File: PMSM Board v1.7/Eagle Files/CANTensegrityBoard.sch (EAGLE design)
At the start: 92 parts, among them IC1 DRV8303, U1 TPS73733-Q1_DRB_8, U10 H1206T500R-10, U2 SN65HVD232_D_8, U3 SN65LVDT348_PW_1, U4 TPS54240_DRC_10, U5 LP38692_NGG_6, U6 DSPIC33EP256MU80, U9 H1206T500R-10

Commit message: Finished v1.7
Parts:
- removed SJ1, SJ4, SJ5, SJ6, SJ7: (no value), jumper:SJ
- added JP1: (no value), ASL:M06DUAL_ROW
- added LED5, LED6: (no value), ASL:LED0805
- added R12, R13: 10k, ASL:RESISTOR0805-RES
- added R14, R15: (no value), ASL:RESISTOR0805-RES
- R1: value (none) -> 1 Ohm
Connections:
- removed net EN_A: U3.ROUT1
- removed net EN_A+: U3.RIN1+
- removed net EN_A-: U3.RIN1
- removed net EN_B: U3.ROUT2
- removed net EN_B+: U3.RIN2+
- removed net EN_B-: U3.RIN2
- removed net EN_C: U3.ROUT3
- removed net EN_C+: U3.RIN3+
- removed net EN_C-: U3.RIN3
- removed net N$27: SJ4.2
- removed net N$29: SJ6.2
- removed net N$30: SJ7.2
- removed net N$33: RN1.1
- removed net N$41: RN1.2
- removed net N$42: RN1.3
- removed net N$43: RN1.4
- new net CH_A+: U$15.6, U3.RIN3+
- new net CH_A-: U$15.5, U3.RIN3
- new net CH_B+: U$15.4, U3.RIN2+
- new net CH_B-: U$15.3, U3.RIN2
- new net CH_I+: U$15.2, U3.RIN1+
- new net CH_I-: U$15.1, U3.RIN1
- new net EXT1: JP1.1, U6.PMWR/RP68/RD4
- new net EXT2: JP1.2, U6.PMBE/RP67/RD3
- new net EXT3: JP1.3, U6.DPH/RP66/RD2
- new net HALL1: U$20.3, U6.PGEC2/SOSCO/C3IN1-/T1CK/RPI62/RC14
- new net HALL2: U$20.4, U6.PGED2/SOSCI/C3IN3-/RPI61/RC13
- new net HALL3: U$20.5, U6.INT0/DMH/RP64/RD0
- new net LED1: RN1.4, U6.AN8/PMA6/RPI40/RB8
- new net LED2: RN1.3, U6.AN9/PMA7//RPI41/RB9
- new net LED3: RN1.2, U6.TMS/AN10/CVREF/PMA13/RPI42/RB10
- new net LED4: RN1.1, U6.TDO/AN11/PMA12/RPI43/RB11
- new net N$11: LED5.C, R15.2
- new net N$17: LED6.C, R14.2
- new net N$23: R12.2, U$19.3
- new net QEI_A: U3.ROUT1, U6.C3IN1+/VCMPST3/RP71/RD7
- new net QEI_B: U3.ROUT2, U6.C3IN2-/RP70/RD6
- new net QEI_I: U3.ROUT3, U6.PMRD/RP69/RD5
- net *SCS: now also U6.C2IN1-/PMA2/RPI121/RG9
- net CANRX: now also U6.SDA2/PMA9/RP100/RF4
- net CANTX: now also U6.SCL2/PMA8/RP101/RF5
- net CAN_H: now also U$14.1, U$19.1
- net CAN_L: now also U$14.2, U$19.2
- net CRNT1: now also U6.TCK/AN12/PMA11/RPI44/RB12
- net CRNT2: now also U6.TDI/AN13/PMA10/RPI45/RB13
- net DC_CAL: now also U6.C2IN3-/SDO2/PMA3/RP120/RG8
- net EN_GATE: now also U6.C1IN1-/SDI2/PMA4/RPI119/RG7
- net GND: now also JP1.4, U$15.7, U$20.2, U6.AVSS, U6.VSS, U6.VSS_2, U6.VSS_3
- net MCLR: now also U6.*MCLR
- net MISO: now also U6.AN31/PWM4H/PMD7/RP87/RE7
- net MOSI: now also U6.C1IN3-/SCK2/PMA5/RP118/RG6
- net N$12: now also R14.1
- net N$24: now also R15.1
- net N$25: now also U6.PGEC3/AN1/VREF-/RPI33/RB1
- net N$28: now also R13.2, U$14.3; no longer SJ5.2
- net N$31: now also U6.VCAP
- net N$5: now also U6.VDD_4; no longer SJ1.2
- net PGC: now also U6.PGED1/AN7/RCV/RPI39/RB7
- net PGD: now also U6.PGEC1/AN6/RPI38/RB6
- net PGND: now also U$16.1, U$16.4, U$18.2
- net PVDD: now also U$16.2, U$16.3
- net PWM1H: now also U6.AN29/PWM3H/PMD5/RP85/RE5
- net PWM1L: now also U6.AN28/PWM3L/PMD4/RP84/RE4
- net PWM2H: now also U6.AN27/PWM2H/PMD3/RPI83/RE3
- net PWM2L: now also U6.AN26/PWM2L/PMD2/RP82/RE2
- net PWM3H: now also U6.AN25/PWM1H/PMD1/RPI81/RE1
- net PWM3L: now also U6.AN24/PWM1L/PMD0/RP80/RE0
- net SCLK: now also U6.AN30/PWM4L/PMD6/RPI86/RE6
- net SH_A: now also U$17.5, U$17.6
- net SH_B: now also U$17.3, U$17.4
- net SH_C: now also U$17.1, U$17.2
- net VCC3V3: now also JP1.6, LED5.A, LED6.A, U$20.1, U6.AVDD, U6.VDD, U6.VDD_2, U6.VDD_3; no longer SJ1.1, SJ4.1, SJ5.1, SJ6.1, SJ7.1
- net VCC5V0: now also JP1.5, U$15.10
- net VCC5V5: now also U$18.1
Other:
- moved on the sheet: C20, R1, RN1, TP6, TP7

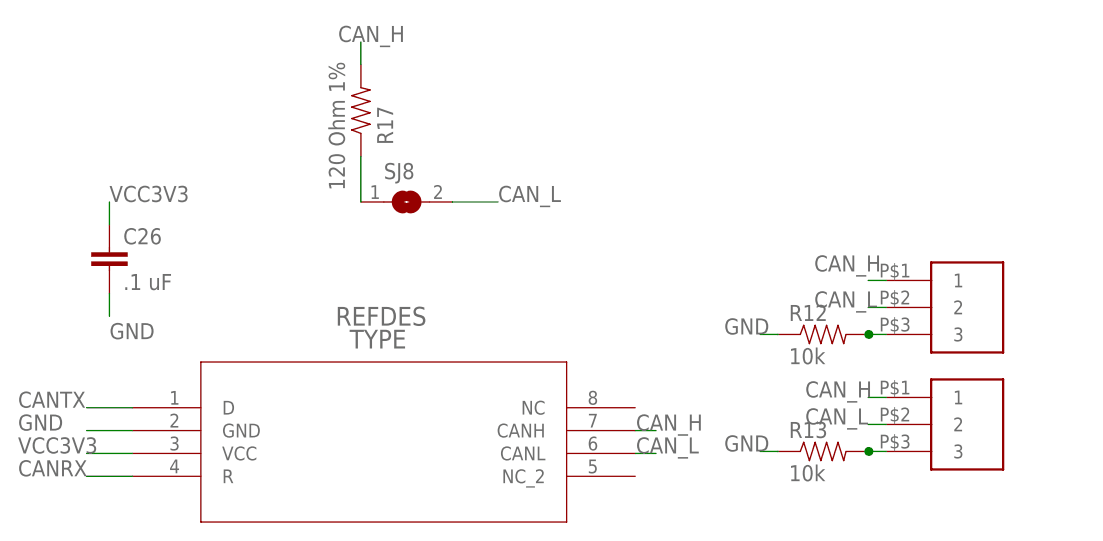
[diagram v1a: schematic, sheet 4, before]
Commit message: Fixed CAN Connector Pinout
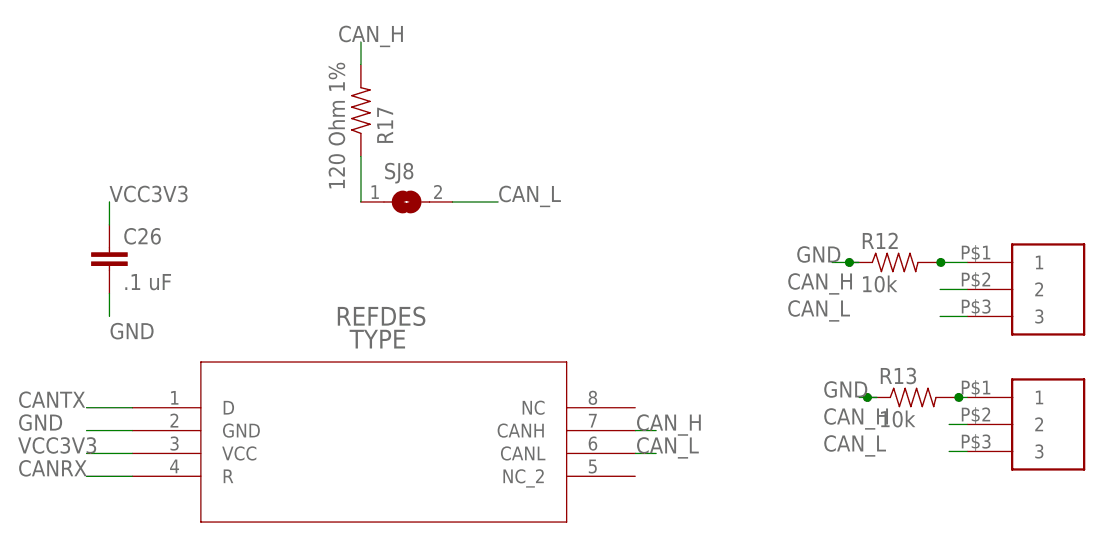
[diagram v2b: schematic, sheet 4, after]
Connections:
- removed net N$23: R12.2, U$19.3
- new net N$27: R12.2, U$19.1
- net CAN_H: now also U$14.2, U$19.2; no longer U$14.1, U$19.1
- net CAN_L: now also U$14.3, U$19.3; no longer U$14.2, U$19.2
- net GND: now also R12.1, R13.1
- net N$28: now also U$14.1; no longer U$14.3
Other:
- moved on the sheet: R12, R13
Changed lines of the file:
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@@
 <setting verticaltext="up"/>
 </settings>
-<grid distance="0.1" unitdist="inch" unit="inch" style="lines" multiple="1" display="no" altdistance="0.01" altunitdist="inch" altunit="inch"/>
+<grid distance="1" unitdist="mm" unit="mm" style="lines" multiple="1" display="no" altdistance="0.1" altunitdist="mm" altunit="mm"/>
 <layers>
 <layer number="1" name="Top" color="4" fill="1" visible="no" active="no"/>
@@
 <instance part="FRAME4" gate="G$1" x="0" y="0"/>
 <instance part="FRAME4" gate="A" x="330" y="0"/>
-<instance part="U$14" gate="G$1" x="280" y="137" rot="R270"/>
-<instance part="U$19" gate="G$1" x="280" y="150" rot="R270"/>
-<instance part="R12" gate="G$1" x="268" y="147"/>
-<instance part="R13" gate="G$1" x="268" y="134"/>
+<instance part="U$14" gate="G$1" x="289" y="137" rot="R270"/>
+<instance part="U$19" gate="G$1" x="289" y="152" rot="R270"/>
+<instance part="R12" gate="G$1" x="276" y="155"/>
+<instance part="R13" gate="G$1" x="278" y="140"/>
 </instances>
 <busses>
@@
 </segment>
 <segment>
-<wire x1="263" y1="147" x2="261" y2="147" width="0.1524" layer="91"/>
-<label x="257" y="147" size="1.778" layer="95"/>
-</segment>
-<segment>
-<wire x1="263" y1="134" x2="261" y2="134" width="0.1524" layer="91"/>
-<label x="257" y="134" size="1.778" layer="95"/>
+<wire x1="272" y1="155" x2="270.92" y2="155" width="0.1524" layer="91"/>
+<label x="265" y="155" size="1.778" layer="95"/>
+<pinref part="R12" gate="G$1" pin="1"/>
+<wire x1="270.92" y1="155" x2="269" y2="155" width="0.1524" layer="91"/>
+<junction x="270.92" y="155"/>
+</segment>
+<segment>
+<wire x1="274" y1="140" x2="272.92" y2="140" width="0.1524" layer="91"/>
+<label x="268" y="140" size="1.778" layer="95"/>
+<pinref part="R13" gate="G$1" pin="1"/>
+<wire x1="272.92" y1="140" x2="272" y2="140" width="0.1524" layer="91"/>
+<junction x="272.92" y="140"/>
 </segment>
 </net>
@@
 </segment>
 <segment>
-<pinref part="U$19" gate="G$1" pin="1"/>
-<wire x1="275" y1="153" x2="273" y2="153" width="0.1524" layer="91"/>
-<label x="267" y="154" size="1.778" layer="95"/>
-</segment>
-<segment>
-<pinref part="U$14" gate="G$1" pin="1"/>
-<wire x1="275" y1="140" x2="273" y2="140" width="0.1524" layer="91"/>
-<label x="266" y="140" size="1.778" layer="95"/>
+<pinref part="U$19" gate="G$1" pin="2"/>
+<wire x1="284" y1="152" x2="281" y2="152" width="0.1524" layer="91"/>
+<label x="264" y="152" size="1.778" layer="95"/>
+</segment>
+<segment>
+<pinref part="U$14" gate="G$1" pin="2"/>
+<wire x1="284" y1="137" x2="282" y2="137" width="0.1524" layer="91"/>
+<label x="268" y="137" size="1.778" layer="95"/>
 </segment>
 </net>
@@
 </segment>
 <segment>
-<pinref part="U$19" gate="G$1" pin="2"/>
-<wire x1="275" y1="150" x2="273" y2="150" width="0.1524" layer="91"/>
-<label x="267" y="150" size="1.778" layer="95"/>
-</segment>
-<segment>
-<pinref part="U$14" gate="G$1" pin="2"/>
-<wire x1="275" y1="137" x2="273" y2="137" width="0.1524" layer="91"/>
-<label x="266" y="137" size="1.778" layer="95"/>
-</segment>
-</net>
-<net name="N$23" class="0">
-<segment>
 <pinref part="U$19" gate="G$1" pin="3"/>
-<wire x1="275" y1="147" x2="273.08" y2="147" width="0.1524" layer="91"/>
+<wire x1="284" y1="149" x2="281" y2="149" width="0.1524" layer="91"/>
+<label x="264" y="149" size="1.778" layer="95"/>
+</segment>
+<segment>
+<pinref part="U$14" gate="G$1" pin="3"/>
+<wire x1="284" y1="134" x2="282" y2="134" width="0.1524" layer="91"/>
+<label x="268" y="134" size="1.778" layer="95"/>
+</segment>
+</net>
+<net name="N$27" class="0">
+<segment>
+<pinref part="U$19" gate="G$1" pin="1"/>
+<wire x1="284" y1="155" x2="281.08" y2="155" width="0.1524" layer="91"/>
 <pinref part="R12" gate="G$1" pin="2"/>
-<wire x1="273.08" y1="147" x2="273" y2="147" width="0.1524" layer="91"/>
-<junction x="273.08" y="147"/>
+<wire x1="281.08" y1="155" x2="281" y2="155" width="0.1524" layer="91"/>
+<junction x="281.08" y="155"/>
 </segment>
 </net>
 <net name="N$28" class="0">
 <segment>
-<pinref part="U$14" gate="G$1" pin="3"/>
-<wire x1="275" y1="134" x2="273.08" y2="134" width="0.1524" layer="91"/>
+<pinref part="U$14" gate="G$1" pin="1"/>
+<wire x1="284" y1="140" x2="283.08" y2="140" width="0.1524" layer="91"/>
 <pinref part="R13" gate="G$1" pin="2"/>
-<wire x1="273.08" y1="134" x2="273" y2="134" width="0.1524" layer="91"/>
-<junction x="273.08" y="134"/>
-</segment>
-</net>
+<wire x1="283.08" y1="140" x2="283" y2="140" width="0.1524" layer="91"/>
+<junction x="283.08" y="140"/>
+</segment>
+</net>

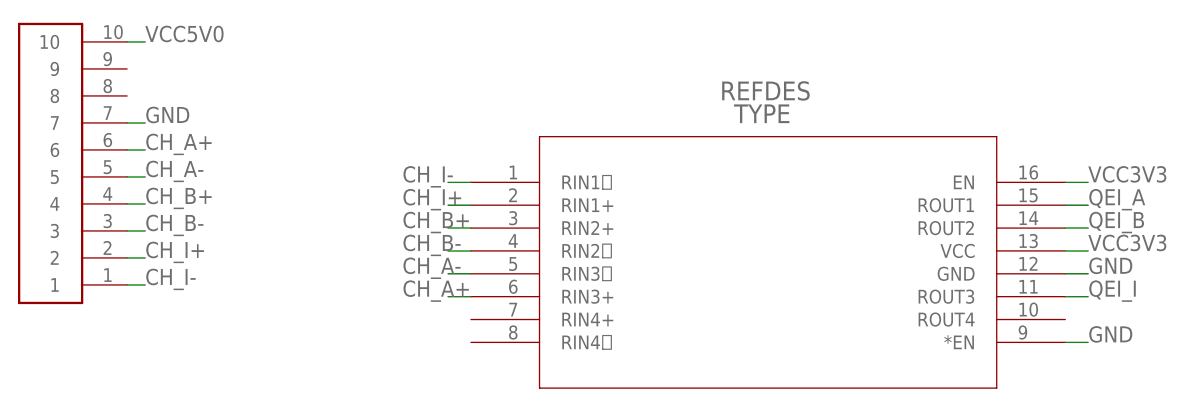
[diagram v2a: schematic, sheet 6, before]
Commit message: Fixed Optical Encoder Output
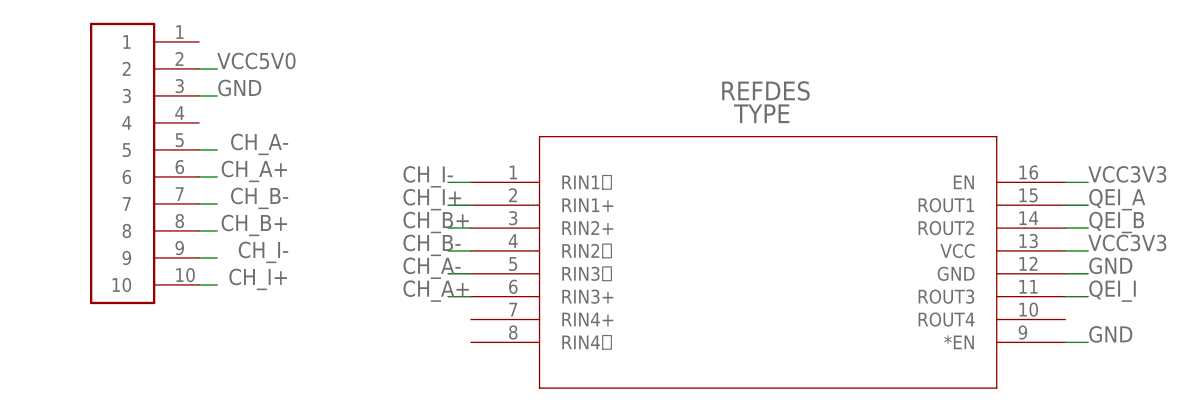
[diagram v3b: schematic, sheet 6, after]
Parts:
- removed U$15: 3M10PIN2500, OpenPMSM:3M10PIN2500
- added U$21: 3M10PIN2500, OpenPMSM:3M10PIN2500
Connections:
- net CH_A+: now also U$21.6; no longer U$15.6
- net CH_A-: now also U$21.5; no longer U$15.5
- net CH_B+: now also U$21.8; no longer U$15.4
- net CH_B-: now also U$21.7; no longer U$15.3
- net CH_I+: now also U$21.10; no longer U$15.2
- net CH_I-: now also U$21.9; no longer U$15.1
- net GND: now also U$21.3; no longer U$15.7
- net VCC5V0: now also U$21.2; no longer U$15.10
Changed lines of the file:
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@@
 <part name="C32" library="SwitcherPowerStage" deviceset="CAP" device="0805" value="1uF"/>
 <part name="U$14" library="OpenPMSM" deviceset="MICROCLASP3" device=""/>
-<part name="U$15" library="OpenPMSM" deviceset="3M10PIN2500" device=""/>
 <part name="U$16" library="OpenPMSM" deviceset="MINIFITJR4PIN" device=""/>
 <part name="U$17" library="OpenPMSM" deviceset="MINIFITJR6PIN" device=""/>
@@
 <part name="LED6" library="ASL" deviceset="LED" device="0805"/>
 <part name="JP1" library="ASL" deviceset="M06" device="DUAL_ROW"/>
+<part name="U$21" library="OpenPMSM" deviceset="3M10PIN2500" device=""/>
 </parts>
 <sheets>
@@
 <instance part="FRAME6" gate="G$1" x="0" y="0"/>
 <instance part="FRAME6" gate="A" x="330" y="0"/>
-<instance part="U$15" gate="G$1" x="160" y="155" rot="R90"/>
+<instance part="U$21" gate="G$1" x="168" y="154" rot="MR270"/>
 </instances>
 <busses>
@@
 <net name="CH_A+" class="0">
 <segment>
-<pinref part="U$15" gate="G$1" pin="6"/>
-<wire x1="165" y1="156" x2="167" y2="156" width="0.1524" layer="91"/>
-<label x="167" y="156" size="1.778" layer="95"/>
-</segment>
-<segment>
 <pinref part="U3" gate="A" pin="RIN3+"/>
 <wire x1="203.2" y1="139.7" x2="200.66" y2="139.7" width="0.1524" layer="91"/>
 <label x="195.58" y="139.7" size="1.778" layer="95"/>
 </segment>
+<segment>
+<wire x1="175" y1="153" x2="173" y2="153" width="0.1524" layer="91"/>
+<label x="183" y="153" size="1.778" layer="95" rot="MR0"/>
+<pinref part="U$21" gate="G$1" pin="6"/>
+</segment>
 </net>
 <net name="CH_A-" class="0">
-<segment>
-<pinref part="U$15" gate="G$1" pin="5"/>
-<wire x1="165" y1="153" x2="167" y2="153" width="0.1524" layer="91"/>
-<label x="167" y="153" size="1.778" layer="95"/>
-</segment>
 <segment>
 <pinref part="U3" gate="A" pin="RIN3"/>
@@
 <label x="195.58" y="142.24" size="1.778" layer="95"/>
 </segment>
+<segment>
+<wire x1="175" y1="156" x2="173" y2="156" width="0.1524" layer="91"/>
+<label x="183" y="156" size="1.778" layer="95" rot="MR0"/>
+<pinref part="U$21" gate="G$1" pin="5"/>
+</segment>
 </net>
 <net name="CH_B+" class="0">
-<segment>
-<pinref part="U$15" gate="G$1" pin="4"/>
-<wire x1="165" y1="150" x2="167" y2="150" width="0.1524" layer="91"/>
-<label x="167" y="150" size="1.778" layer="95"/>
-</segment>
 <segment>
 <pinref part="U3" gate="A" pin="RIN2+"/>
@@
 <label x="195.58" y="147.32" size="1.778" layer="95"/>
 </segment>
+<segment>
+<wire x1="175" y1="147" x2="173" y2="147" width="0.1524" layer="91"/>
+<label x="183" y="147" size="1.778" layer="95" rot="MR0"/>
+<pinref part="U$21" gate="G$1" pin="8"/>
+</segment>
 </net>
 <net name="CH_B-" class="0">
-<segment>
-<pinref part="U$15" gate="G$1" pin="3"/>
-<wire x1="165" y1="147" x2="167" y2="147" width="0.1524" layer="91"/>
-<label x="167" y="147" size="1.778" layer="95"/>
-</segment>
 <segment>
 <pinref part="U3" gate="A" pin="RIN2"/>
@@
 <label x="195.58" y="144.78" size="1.778" layer="95"/>
 </segment>
+<segment>
+<wire x1="175" y1="150" x2="173" y2="150" width="0.1524" layer="91"/>
+<label x="183" y="150" size="1.778" layer="95" rot="MR0"/>
+<pinref part="U$21" gate="G$1" pin="7"/>
+</segment>
 </net>
 <net name="CH_I+" class="0">
-<segment>
-<pinref part="U$15" gate="G$1" pin="2"/>
-<wire x1="165" y1="144" x2="167" y2="144" width="0.1524" layer="91"/>
-<label x="167" y="144" size="1.778" layer="95"/>
-</segment>
 <segment>
 <pinref part="U3" gate="A" pin="RIN1+"/>
@@
 <label x="195.58" y="149.86" size="1.778" layer="95"/>
 </segment>
+<segment>
+<wire x1="175" y1="141" x2="173" y2="141" width="0.1524" layer="91"/>
+<label x="183" y="141" size="1.778" layer="95" rot="MR0"/>
+<pinref part="U$21" gate="G$1" pin="10"/>
+</segment>
 </net>
 <net name="CH_I-" class="0">
-<segment>
-<pinref part="U$15" gate="G$1" pin="1"/>
-<wire x1="165" y1="141" x2="167" y2="141" width="0.1524" layer="91"/>
-<label x="167" y="141" size="1.778" layer="95"/>
-</segment>
 <segment>
 <pinref part="U3" gate="A" pin="RIN1"/>
@@
 <label x="195.58" y="152.4" size="1.778" layer="95"/>
 </segment>
+<segment>
+<wire x1="175" y1="144" x2="173" y2="144" width="0.1524" layer="91"/>
+<label x="183" y="144" size="1.778" layer="95" rot="MR0"/>
+<pinref part="U$21" gate="G$1" pin="9"/>
+</segment>
 </net>
 <net name="VCC3V3" class="3">
@@
 </segment>
 <segment>
-<pinref part="U$15" gate="G$1" pin="7"/>
-<wire x1="165" y1="159" x2="167" y2="159" width="0.1524" layer="91"/>
-<label x="167" y="159" size="1.778" layer="95"/>
+<pinref part="U$21" gate="G$1" pin="3"/>
+<wire x1="173" y1="162" x2="175" y2="162" width="0.1524" layer="91"/>
+<label x="175" y="162" size="1.778" layer="95"/>
 </segment>
 </net>
 <net name="VCC5V0" class="0">
 <segment>
-<pinref part="U$15" gate="G$1" pin="10"/>
-<wire x1="165" y1="168" x2="167" y2="168" width="0.1524" layer="91"/>
-<label x="167" y="168" size="1.778" layer="95"/>
-</segment>
-</net>
+<pinref part="U$21" gate="G$1" pin="2"/>
+<wire x1="173" y1="165" x2="175" y2="165" width="0.1524" layer="91"/>
+<label x="175" y="165" size="1.778" layer="95"/>
+</segment>
+</net>

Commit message: Choring up code for v1.7.
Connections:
- removed net N$5: U6.VDD_4
- net PGC: now also U6.PGEC1/AN6/RPI38/RB6; no longer U6.PGED1/AN7/RCV/RPI39/RB7
- net PGD: now also U6.PGED1/AN7/RCV/RPI39/RB7; no longer U6.PGEC1/AN6/RPI38/RB6
- net VCC3V3: now also U6.VDD_4
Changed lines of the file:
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@@
 <?xml version="1.0" encoding="utf-8"?>
 <!DOCTYPE eagle SYSTEM "eagle.dtd">
-<eagle version="6.4">
+<eagle version="6.5.0">
 <drawing>
 <settings>
@@
 <setting verticaltext="up"/>
 </settings>
-<grid distance="1" unitdist="mm" unit="mm" style="lines" multiple="1" display="no" altdistance="0.1" altunitdist="mm" altunit="mm"/>
+<grid distance="0.1" unitdist="inch" unit="inch" style="lines" multiple="1" display="no" altdistance="0.01" altunitdist="inch" altunit="inch"/>
 <layers>
 <layer number="1" name="Top" color="4" fill="1" visible="no" active="no"/>
@@
 </segment>
 <segment>
+<pinref part="U6" gate="A" pin="PGED1/AN7/RCV/RPI39/RB7"/>
+<wire x1="114.3" y1="144.78" x2="111.76" y2="144.78" width="0.1524" layer="91"/>
+<label x="109.22" y="144.78" size="1.778" layer="95"/>
+</segment>
+</net>
+<net name="PGC" class="0">
+<segment>
+<wire x1="62.94" y1="162.58" x2="70.56" y2="162.58" width="0.1524" layer="91"/>
+<label x="62.94" y="162.58" size="1.778" layer="95"/>
+<pinref part="JP3" gate="G$1" pin="5"/>
+</segment>
+<segment>
 <pinref part="U6" gate="A" pin="PGEC1/AN6/RPI38/RB6"/>
 <wire x1="114.3" y1="147.32" x2="111.76" y2="147.32" width="0.1524" layer="91"/>
 <label x="109.22" y="147.32" size="1.778" layer="95"/>
-</segment>
-</net>
-<net name="PGC" class="0">
-<segment>
-<wire x1="62.94" y1="162.58" x2="70.56" y2="162.58" width="0.1524" layer="91"/>
-<label x="62.94" y="162.58" size="1.778" layer="95"/>
-<pinref part="JP3" gate="G$1" pin="5"/>
-</segment>
-<segment>
-<pinref part="U6" gate="A" pin="PGED1/AN7/RCV/RPI39/RB7"/>
-<wire x1="114.3" y1="144.78" x2="111.76" y2="144.78" width="0.1524" layer="91"/>
-<label x="109.22" y="144.78" size="1.778" layer="95"/>
 </segment>
 </net>
@@
 <pinref part="JP1" gate="G$1" pin="6"/>
 <wire x1="325.12" y1="96.52" x2="325.12" y2="99.06" width="0.1524" layer="91"/>
+</segment>
+<segment>
+<pinref part="U6" gate="A" pin="VDD_4"/>
+<wire x1="312.42" y1="121.92" x2="302.26" y2="121.92" width="0.1524" layer="91"/>
 </segment>
 </net>
@@
 </segment>
 </net>
-<net name="N$5" class="0">
-<segment>
-<pinref part="U6" gate="A" pin="VDD_4"/>
-<wire x1="312.42" y1="121.92" x2="302.26" y2="121.92" width="0.1524" layer="91"/>
-</segment>
-</net>
